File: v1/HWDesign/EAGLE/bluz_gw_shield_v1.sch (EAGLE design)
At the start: 19 parts, among them Q1 FC-12M, U2 MDBT40SMD, U3 SST25VF040B-S2, U4 SPARK_CORE

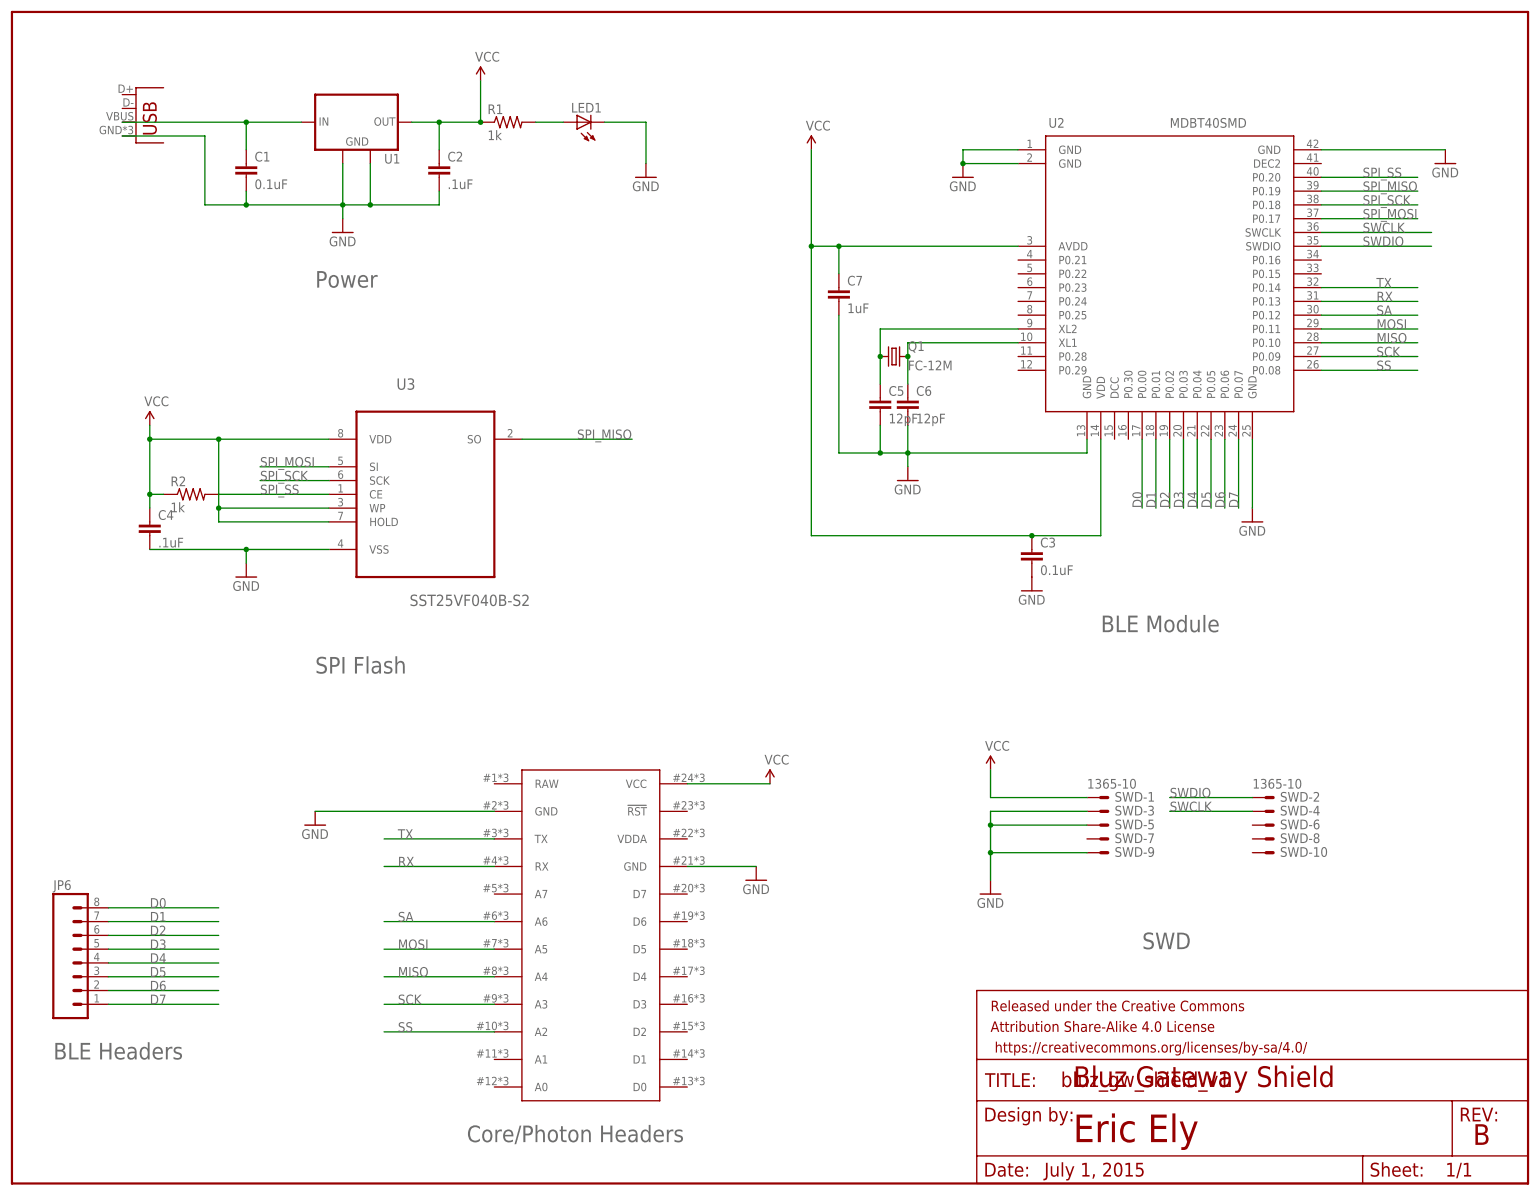
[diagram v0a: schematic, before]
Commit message: add reset button
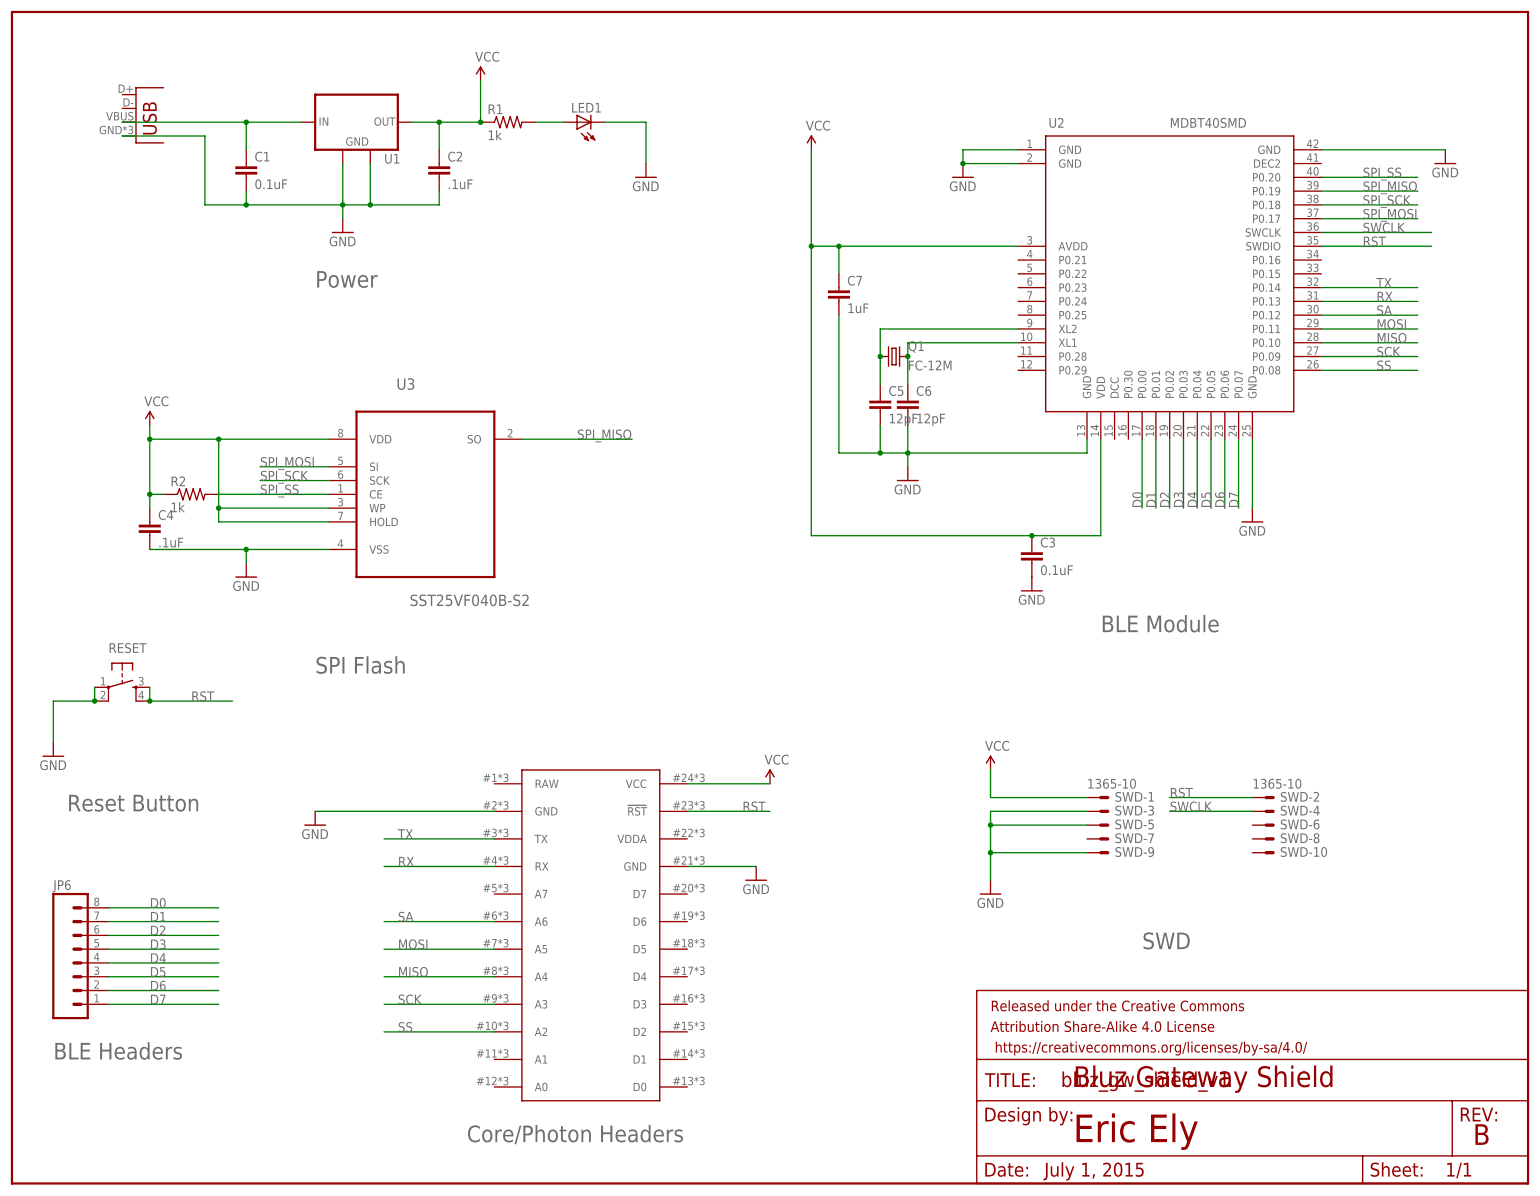
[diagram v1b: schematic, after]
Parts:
- added RESET: (no value), Spark:TAC_SWITCHSMD
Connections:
- removed net SWDIO: SWD-2.S, U2.SWDIO
- new net RST: RESET.3, RESET.4, SWD-2.S, U2.SWDIO, U4.!RST
- net GND: now also RESET.1, RESET.2
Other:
- note added: "Reset Button"
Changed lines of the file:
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@@
 <?xml version="1.0" encoding="utf-8"?>
 <!DOCTYPE eagle SYSTEM "eagle.dtd">
-<eagle version="6.5.0">
+<eagle version="7.3.0">
 <drawing>
 <settings>
@@
 <part name="GND2" library="SparkFun-Aesthetics" deviceset="GND" device=""/>
 <part name="FRAME1" library="SparkFun-Aesthetics" deviceset="FRAME-LETTER" device=""/>
+<part name="RESET" library="Spark" deviceset="TAC_SWITCH" device="SMD"/>
+<part name="GND12" library="SparkFun-Aesthetics" deviceset="GND" device=""/>
 </parts>
 <sheets>
@@
 <text x="269.24" y="7.112" size="3.81" layer="94">B</text>
 <text x="55.88" y="93.98" size="3.048" layer="95">SPI Flash</text>
+<text x="10.16" y="68.58" size="3.048" layer="95">Reset Button</text>
 </plain>
 <instances>
@@
 <attribute name="SHEET" x="264.16" y="1.27" size="2.54" layer="94" font="vector"/>
 </instance>
+<instance part="RESET" gate="S" x="20.32" y="91.44"/>
+<instance part="GND12" gate="1" x="7.62" y="78.74"/>
 </instances>
 <busses>
@@
 <wire x1="55.88" y1="68.58" x2="88.9" y2="68.58" width="0.1524" layer="91"/>
 </segment>
+<segment>
+<pinref part="RESET" gate="S" pin="1"/>
+<pinref part="RESET" gate="S" pin="2"/>
+<wire x1="15.24" y1="91.44" x2="15.24" y2="88.9" width="0.1524" layer="91"/>
+<wire x1="15.24" y1="88.9" x2="7.62" y2="88.9" width="0.1524" layer="91"/>
+<wire x1="7.62" y1="88.9" x2="7.62" y2="81.28" width="0.1524" layer="91"/>
+<junction x="15.24" y="88.9"/>
+<pinref part="GND12" gate="1" pin="GND"/>
+</segment>
 </net>
 <net name="VCC" class="0">
@@
 </segment>
 </net>
-<net name="SWDIO" class="0">
-<segment>
-<pinref part="U2" gate="G$1" pin="SWDIO"/>
-<wire x1="241.3" y1="172.72" x2="261.62" y2="172.72" width="0.1524" layer="91"/>
-<label x="248.92" y="172.72" size="1.778" layer="95"/>
-</segment>
-<segment>
-<pinref part="SWD" gate="-2" pin="S"/>
-<wire x1="228.6" y1="71.12" x2="213.36" y2="71.12" width="0.1524" layer="91"/>
-<label x="213.36" y="71.12" size="1.778" layer="95"/>
-</segment>
-</net>
 <net name="SS" class="0">
 <segment>
@@
 </segment>
 </net>
+<net name="RST" class="0">
+<segment>
+<pinref part="U2" gate="G$1" pin="SWDIO"/>
+<wire x1="241.3" y1="172.72" x2="261.62" y2="172.72" width="0.1524" layer="91"/>
+<label x="248.92" y="172.72" size="1.778" layer="95"/>
+</segment>
+<segment>
+<pinref part="SWD" gate="-2" pin="S"/>
+<wire x1="228.6" y1="71.12" x2="213.36" y2="71.12" width="0.1524" layer="91"/>
+<label x="213.36" y="71.12" size="1.778" layer="95"/>
+</segment>
+<segment>
+<pinref part="U4" gate="G$1" pin="!RST"/>
+<wire x1="124.46" y1="68.58" x2="139.7" y2="68.58" width="0.1524" layer="91"/>
+<label x="134.62" y="68.58" size="1.778" layer="95"/>
+</segment>
+<segment>
+<pinref part="RESET" gate="S" pin="3"/>
+<pinref part="RESET" gate="S" pin="4"/>
+<wire x1="25.4" y1="91.44" x2="25.4" y2="88.9" width="0.1524" layer="91"/>
+<wire x1="25.4" y1="88.9" x2="40.64" y2="88.9" width="0.1524" layer="91"/>
+<junction x="25.4" y="88.9"/>
+<label x="33.02" y="88.9" size="1.778" layer="95"/>
+</segment>
+</net>

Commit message: updated BOM, was missing a few things
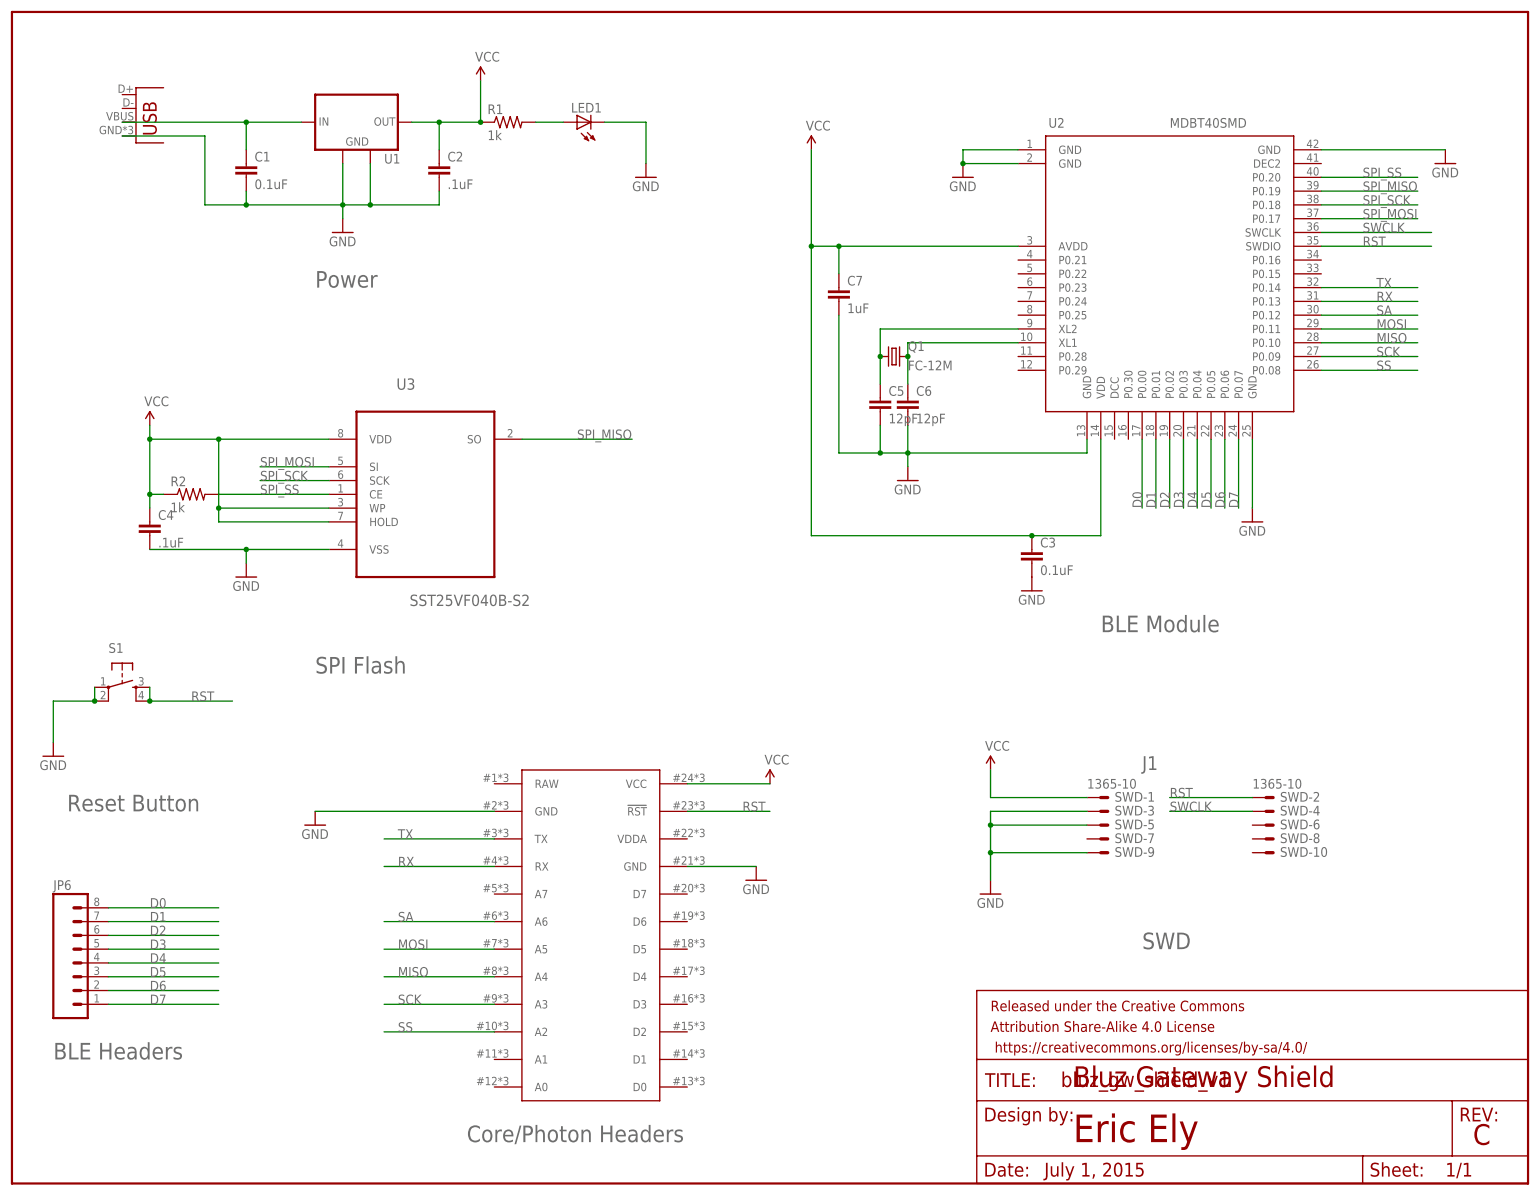
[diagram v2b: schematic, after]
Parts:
- renumbered JP3 to J2, RESET to S1
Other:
- note added: "C"
- note added: "J1"
- note removed: "B"
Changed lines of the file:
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@@
 <part name="C1" library="SparkFun-Passives" deviceset="CAP" device="0603-CAP" value="0.1uF"/>
 <part name="U1" library="Spark" deviceset="MCP1825S" device="-SOT223"/>
-<part name="JP3" library="SparkFun-Connectors" deviceset="USB" device="-MICROB"/>
+<part name="J2" library="SparkFun-Connectors" deviceset="USB" device="-MICROB"/>
 <part name="SWD" library="con-leotronics" deviceset="1365-10" device=""/>
 <part name="C3" library="SparkFun-Capacitors" deviceset="CAP" device="0603-CAP" value="0.1uF"/>
@@
 <part name="GND2" library="SparkFun-Aesthetics" deviceset="GND" device=""/>
 <part name="FRAME1" library="SparkFun-Aesthetics" deviceset="FRAME-LETTER" device=""/>
-<part name="RESET" library="Spark" deviceset="TAC_SWITCH" device="SMD"/>
+<part name="S1" library="Spark" deviceset="TAC_SWITCH" device="SMD"/>
 <part name="GND12" library="SparkFun-Aesthetics" deviceset="GND" device=""/>
 </parts>
@@
 <text x="195.58" y="17.78" size="3.81" layer="94">Bluz Gateway Shield</text>
 <text x="190.246" y="1.27" size="2.54" layer="94">July 1, 2015</text>
-<text x="269.24" y="7.112" size="3.81" layer="94">B</text>
+<text x="269.24" y="7.112" size="3.81" layer="94">C</text>
 <text x="55.88" y="93.98" size="3.048" layer="95">SPI Flash</text>
 <text x="10.16" y="68.58" size="3.048" layer="95">Reset Button</text>
+<text x="208.28" y="76.2" size="2.54" layer="95">J1</text>
 </plain>
 <instances>
@@
 <instance part="C1" gate="G$1" x="43.18" y="185.42"/>
 <instance part="U1" gate="G$1" x="63.5" y="195.58"/>
-<instance part="JP3" gate="G$1" x="22.86" y="193.04"/>
+<instance part="J2" gate="G$1" x="22.86" y="193.04"/>
 <instance part="SWD" gate="-1" x="200.66" y="71.12"/>
 <instance part="SWD" gate="-2" x="231.14" y="71.12"/>
@@
 <attribute name="SHEET" x="264.16" y="1.27" size="2.54" layer="94" font="vector"/>
 </instance>
-<instance part="RESET" gate="S" x="20.32" y="91.44"/>
+<instance part="S1" gate="S" x="20.32" y="91.44"/>
 <instance part="GND12" gate="1" x="7.62" y="78.74"/>
 </instances>
@@
 <net name="N$1" class="0">
 <segment>
-<pinref part="JP3" gate="G$1" pin="VBUS"/>
+<pinref part="J2" gate="G$1" pin="VBUS"/>
 <pinref part="U1" gate="G$1" pin="IN"/>
 <wire x1="20.32" y1="195.58" x2="43.18" y2="195.58" width="0.1524" layer="91"/>
@@
 <wire x1="35.56" y1="180.34" x2="43.18" y2="180.34" width="0.1524" layer="91"/>
 <junction x="43.18" y="180.34"/>
-<pinref part="JP3" gate="G$1" pin="GND"/>
+<pinref part="J2" gate="G$1" pin="GND"/>
 <wire x1="35.56" y1="193.04" x2="20.32" y2="193.04" width="0.1524" layer="91"/>
 <pinref part="C2" gate="G$1" pin="2"/>
@@
 </segment>
 <segment>
-<pinref part="RESET" gate="S" pin="1"/>
-<pinref part="RESET" gate="S" pin="2"/>
+<pinref part="S1" gate="S" pin="1"/>
+<pinref part="S1" gate="S" pin="2"/>
 <wire x1="15.24" y1="91.44" x2="15.24" y2="88.9" width="0.1524" layer="91"/>
 <wire x1="15.24" y1="88.9" x2="7.62" y2="88.9" width="0.1524" layer="91"/>
@@
 </segment>
 <segment>
-<pinref part="RESET" gate="S" pin="3"/>
-<pinref part="RESET" gate="S" pin="4"/>
+<pinref part="S1" gate="S" pin="3"/>
+<pinref part="S1" gate="S" pin="4"/>
 <wire x1="25.4" y1="91.44" x2="25.4" y2="88.9" width="0.1524" layer="91"/>
 <wire x1="25.4" y1="88.9" x2="40.64" y2="88.9" width="0.1524" layer="91"/>
